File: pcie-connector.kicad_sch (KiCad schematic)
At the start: 6 parts, among them J9 Edge_Conn_Bus_PCIe_x4, SW6 SW_CVS-02B

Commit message: [#65754] Rename project
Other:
- title: SO-DIMM DDR5 Tester -> RDIMM DDR5 Tester
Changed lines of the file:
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@@
   (paper "A3")
   (title_block
-    (title "SO-DIMM DDR5 Tester")
-    (date "2024-04-23")
-    (rev "1.2.0")
+    (title "RDIMM DDR5 Tester")
+    (date "2024-09-26")
+    (rev "2.0.0")
     (comment 1 "www.antmicro.com")
     (comment 2 "Antmicro Ltd")
@@
     (pin "SH")
     (instances
-      (project "rdimm-ddr5-tester-ultrascale-plus"
+      (project "data-center-rdimm-ddr5-tester"
         (path "/1faa6543-e26a-4449-8bac-ee14b9f19e5f/fea793c3-bc28-42ef-95e7-45c2f3eee090"
           (reference "SW6") (unit 1)
@@
     (pin "1")
     (instances
-      (project "rdimm-ddr5-tester-ultrascale-plus"
+      (project "data-center-rdimm-ddr5-tester"
         (path "/1faa6543-e26a-4449-8bac-ee14b9f19e5f/fea793c3-bc28-42ef-95e7-45c2f3eee090"
           (reference "#PWR0398") (unit 1)
@@
     (pin "1")
     (instances
-      (project "rdimm-ddr5-tester-ultrascale-plus"
+      (project "data-center-rdimm-ddr5-tester"
         (path "/1faa6543-e26a-4449-8bac-ee14b9f19e5f/fea793c3-bc28-42ef-95e7-45c2f3eee090"
           (reference "#PWR0422") (unit 1)
@@
     (pin "1")
     (instances
-      (project "rdimm-ddr5-tester-ultrascale-plus"
+      (project "data-center-rdimm-ddr5-tester"
         (path "/1faa6543-e26a-4449-8bac-ee14b9f19e5f/fea793c3-bc28-42ef-95e7-45c2f3eee090"
           (reference "#PWR0402") (unit 1)
@@
     (pin "1")
     (instances
-      (project "rdimm-ddr5-tester-ultrascale-plus"
+      (project "data-center-rdimm-ddr5-tester"
         (path "/1faa6543-e26a-4449-8bac-ee14b9f19e5f/fea793c3-bc28-42ef-95e7-45c2f3eee090"
           (reference "#PWR0403") (unit 1)
@@
     (pin "2")
     (instances
-      (project "rdimm-ddr5-tester-ultrascale-plus"
+      (project "data-center-rdimm-ddr5-tester"
         (path "/1faa6543-e26a-4449-8bac-ee14b9f19e5f/fea793c3-bc28-42ef-95e7-45c2f3eee090"
           (reference "C225") (unit 1)
@@
     (pin "1")
     (instances
-      (project "rdimm-ddr5-tester-ultrascale-plus"
+      (project "data-center-rdimm-ddr5-tester"
         (path "/1faa6543-e26a-4449-8bac-ee14b9f19e5f/fea793c3-bc28-42ef-95e7-45c2f3eee090"
           (reference "#PWR0400") (unit 1)
@@
     (pin "2")
     (instances
-      (project "rdimm-ddr5-tester-ultrascale-plus"
+      (project "data-center-rdimm-ddr5-tester"
         (path "/1faa6543-e26a-4449-8bac-ee14b9f19e5f/fea793c3-bc28-42ef-95e7-45c2f3eee090"
           (reference "C224") (unit 1)
@@
     (pin "1")
     (instances
-      (project "rdimm-ddr5-tester-ultrascale-plus"
+      (project "data-center-rdimm-ddr5-tester"
         (path "/1faa6543-e26a-4449-8bac-ee14b9f19e5f/fea793c3-bc28-42ef-95e7-45c2f3eee090"
           (reference "#PWR0401") (unit 1)
@@
     (pin "1")
     (instances
-      (project "rdimm-ddr5-tester-ultrascale-plus"
+      (project "data-center-rdimm-ddr5-tester"
         (path "/1faa6543-e26a-4449-8bac-ee14b9f19e5f/fea793c3-bc28-42ef-95e7-45c2f3eee090"
           (reference "#PWR0399") (unit 1)
@@
     (pin "B9")
     (instances
-      (project "rdimm-ddr5-tester-ultrascale-plus"
+      (project "data-center-rdimm-ddr5-tester"
         (path "/1faa6543-e26a-4449-8bac-ee14b9f19e5f/fea793c3-bc28-42ef-95e7-45c2f3eee090"
           (reference "J9") (unit 1)
@@
     (pin "2")
     (instances
-      (project "rdimm-ddr5-tester-ultrascale-plus"
+      (project "data-center-rdimm-ddr5-tester"
         (path "/1faa6543-e26a-4449-8bac-ee14b9f19e5f/fea793c3-bc28-42ef-95e7-45c2f3eee090"
           (reference "R191") (unit 1)
@@
     (pin "2")
     (instances
-      (project "rdimm-ddr5-tester-ultrascale-plus"
+      (project "data-center-rdimm-ddr5-tester"
         (path "/1faa6543-e26a-4449-8bac-ee14b9f19e5f/fea793c3-bc28-42ef-95e7-45c2f3eee090"
           (reference "R192") (unit 1)

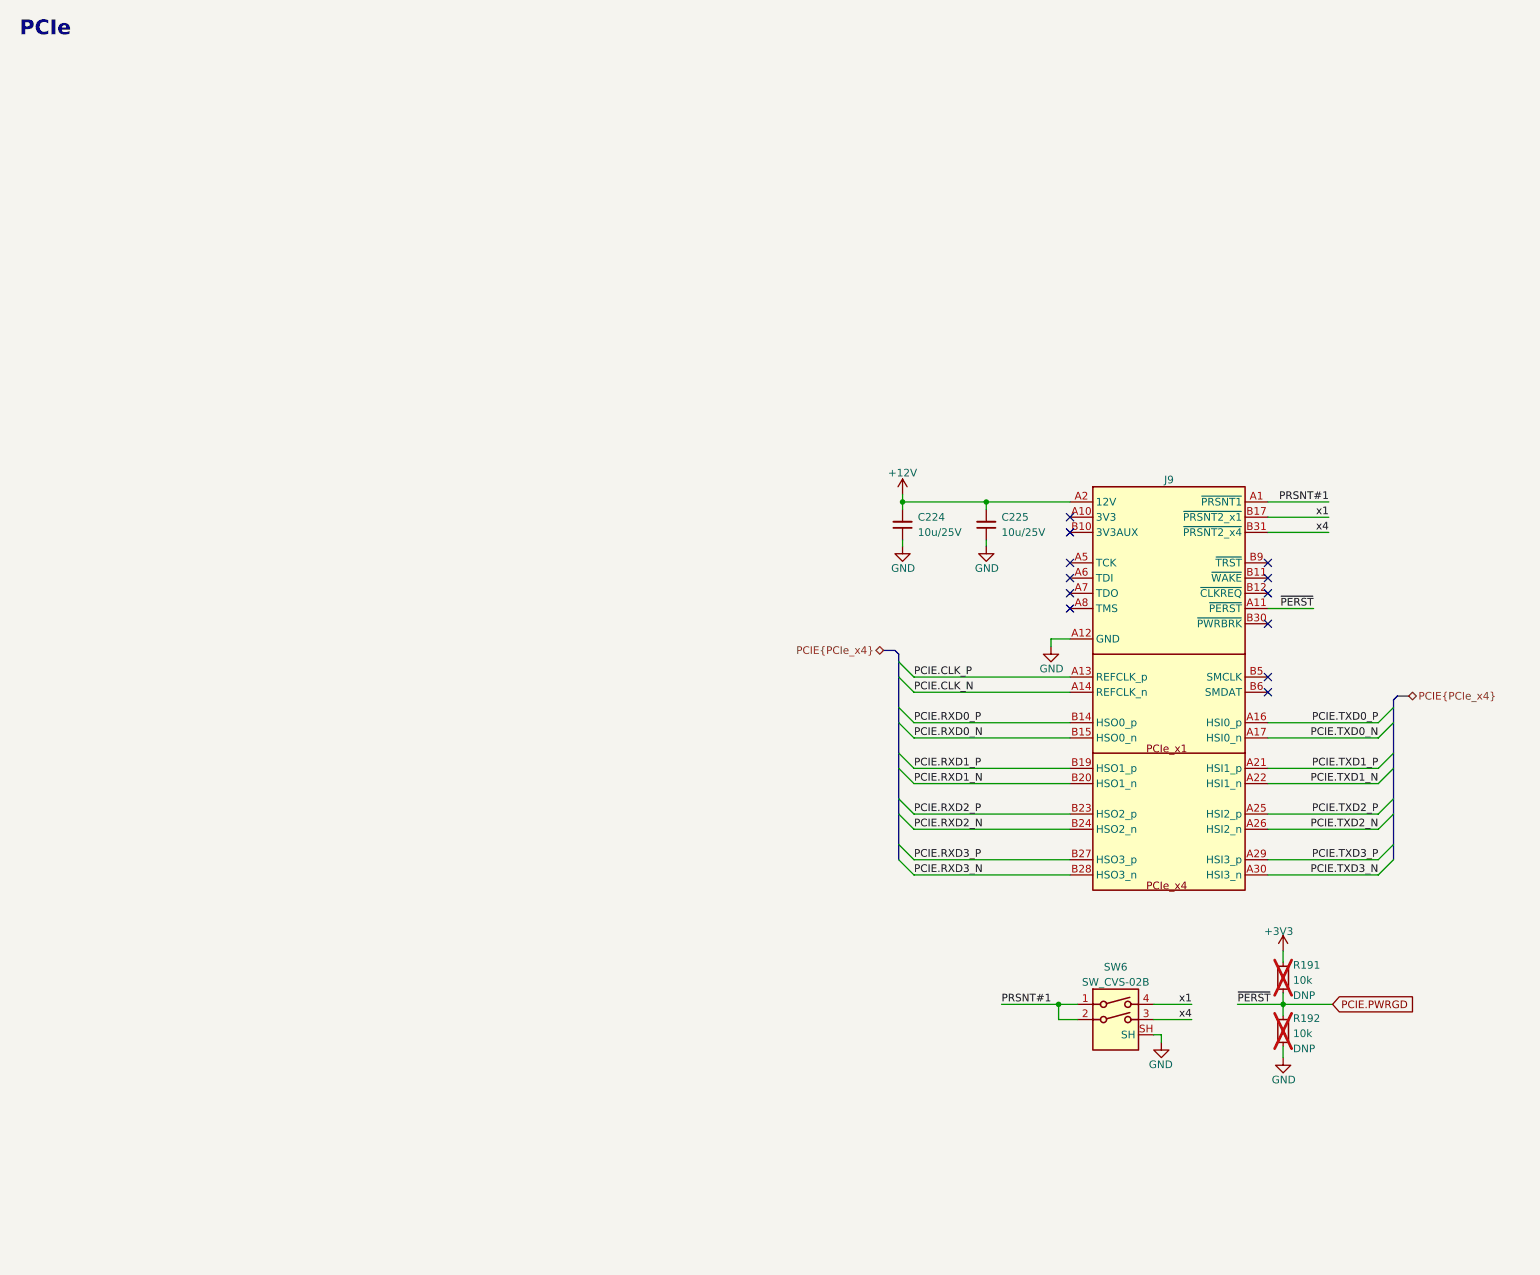
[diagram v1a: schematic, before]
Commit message: [#66312] Connect x8 PCIe
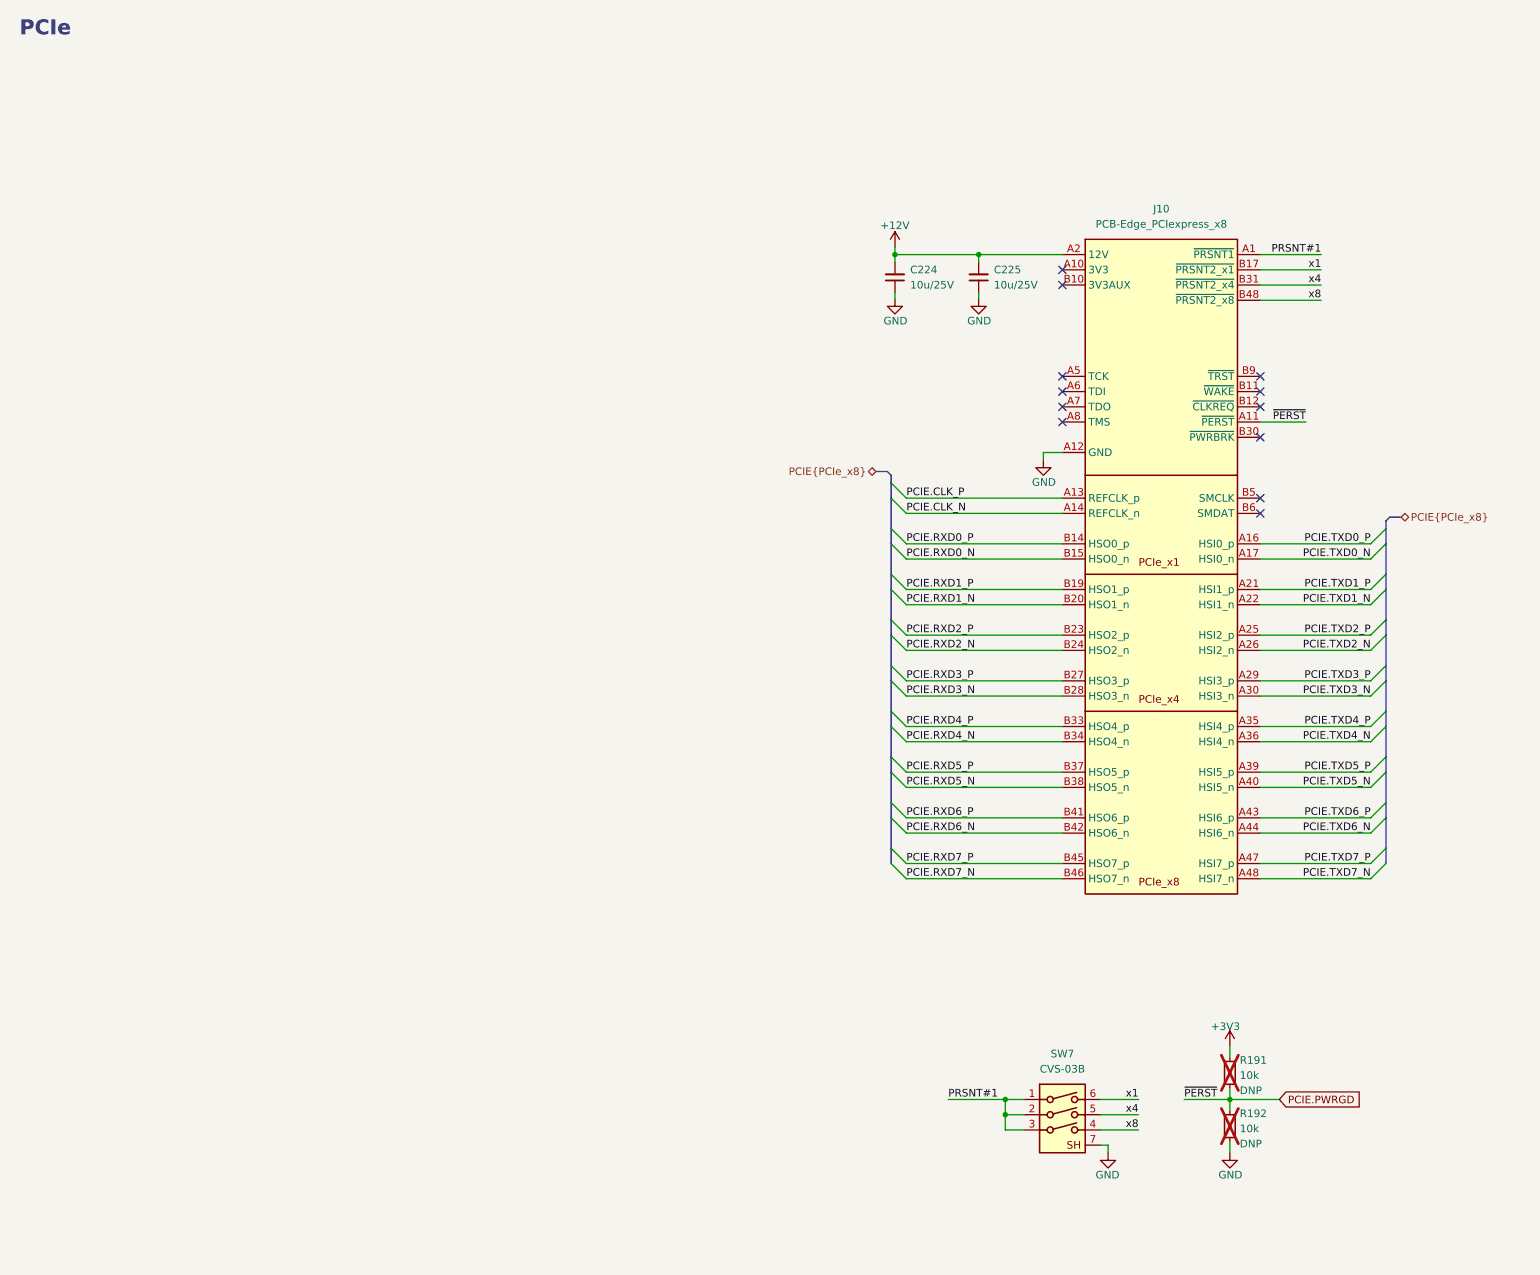
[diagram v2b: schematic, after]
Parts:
- removed J9: Edge_Conn_Bus_PCIe_x4, antmicro-footprints:Edge_Conn_Bus_PCIexpress_x4, symbol antmicroPciConnectors:Edge_Conn_Bus_PCIe_x4
- removed SW6: SW_CVS-02B, antmicro-footprints:SW_DIP_SPSTx02_Slide_Copal_CVS-02xB_W5.9mm_P1mm, symbol antmicroSlideSwitches:SW_CVS-02B
- added J10: PCB-Edge_PCIexpress_x8, antmicro-footprints:PCB-Edge_PCIexpress_x8, symbol antmicroEdgeConnectors:PCB-Edge_PCIexpress_x8
- added SW7: CVS-03B, antmicro-footprints:SW_DIP_SPSTx03_Slide_Copal_CVS-03xB_W5.9mm_P1mm, symbol antmicroSlideSwitches:CVS-03B
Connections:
- net +12V: now also J10.A2 (12V), J10.A3 (12V), J10.B1 (12V), J10.B2 (12V), J10.B3 (12V)
- net GND: now also J10.A12 (GND), J10.A15 (GND), J10.A18 (GND), J10.A20 (GND), J10.A23 (GND), J10.A24 (GND), J10.A27 (GND), J10.A28 (GND), J10.A31 (GND), J10.A34 (GND), J10.A37 (GND), J10.A38 (GND), J10.A4 (GND), J10.A41 (GND), J10.A42 (GND), J10.A45 (GND), J10.A46 (GND), J10.A49 (GND), J10.B13 (GND), J10.B16 (GND), J10.B18 (GND), J10.B21 (GND), J10.B22 (GND), J10.B25 (GND), J10.B26 (GND), J10.B29 (GND), J10.B32 (GND), J10.B35 (GND), J10.B36 (GND), J10.B39 (GND), J10.B4 (GND), J10.B40 (GND), J10.B43 (GND), J10.B44 (GND), J10.B47 (GND), J10.B49 (GND), J10.B7 (GND), SW7.7
- net PCIE.CLK_N: now also J10.A14 (REFCLK_n)
- net PCIE.CLK_P: now also J10.A13 (REFCLK_p)
- net PCIE.PWRGD: now also J10.A11 (~{PERST})
- net PCIE.RXD0_N: now also J10.B15 (HSO0_n)
- net PCIE.RXD0_P: now also J10.B14 (HSO0_p)
- net PCIE.RXD1_N: now also J10.B20 (HSO1_n)
- net PCIE.RXD1_P: now also J10.B19 (HSO1_p)
- net PCIE.RXD2_N: now also J10.B24 (HSO2_n)
- net PCIE.RXD2_P: now also J10.B23 (HSO2_p)
- net PCIE.RXD3_N: now also J10.B28 (HSO3_n)
- net PCIE.RXD3_P: now also J10.B27 (HSO3_p)
- net PCIE.TXD0_N: now also J10.A17 (HSI0_n)
- net PCIE.TXD0_P: now also J10.A16 (HSI0_p)
- net PCIE.TXD1_N: now also J10.A22 (HSI1_n)
- net PCIE.TXD1_P: now also J10.A21 (HSI1_p)
- net PCIE.TXD2_N: now also J10.A26 (HSI2_n)
- net PCIE.TXD2_P: now also J10.A25 (HSI2_p)
- net PCIE.TXD3_N: now also J10.A30 (HSI3_n)
- net PCIE.TXD3_P: now also J10.A29 (HSI3_p)
- net PRSNT#1: now also J10.A1 (~{PRSNT1}), SW7.1, SW7.2, SW7.3
- net x1: now also J10.B17 (~{PRSNT2_x1}), SW7.6
- net x4: now also J10.B31 (~{PRSNT2_x4}), SW7.5
- new net: J10.A10 (3V3), J10.A9 (3V3), J10.B8 (3V3)
- new net PCIE.RXD4_N: J10.B34 (HSO4_n)
- new net PCIE.RXD4_P: J10.B33 (HSO4_p)
- new net PCIE.RXD5_N: J10.B38 (HSO5_n)
- new net PCIE.RXD5_P: J10.B37 (HSO5_p)
- new net PCIE.RXD6_N: J10.B42 (HSO6_n)
- new net PCIE.RXD6_P: J10.B41 (HSO6_p)
- new net PCIE.RXD7_N: J10.B46 (HSO7_n)
- new net PCIE.RXD7_P: J10.B45 (HSO7_p)
- new net PCIE.TXD4_N: J10.A36 (HSI4_n)
- new net PCIE.TXD4_P: J10.A35 (HSI4_p)
- new net PCIE.TXD5_N: J10.A40 (HSI5_n)
- new net PCIE.TXD5_P: J10.A39 (HSI5_p)
- new net PCIE.TXD6_N: J10.A44 (HSI6_n)
- new net PCIE.TXD6_P: J10.A43 (HSI6_p)
- new net PCIE.TXD7_N: J10.A48 (HSI7_n)
- new net PCIE.TXD7_P: J10.A47 (HSI7_p)
- new net x8: J10.B48 (~{PRSNT2_x8}), SW7.4
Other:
- moved on the sheet: C224, C225, R191, R192

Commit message: [#67725] Clean-up PCIe sheet
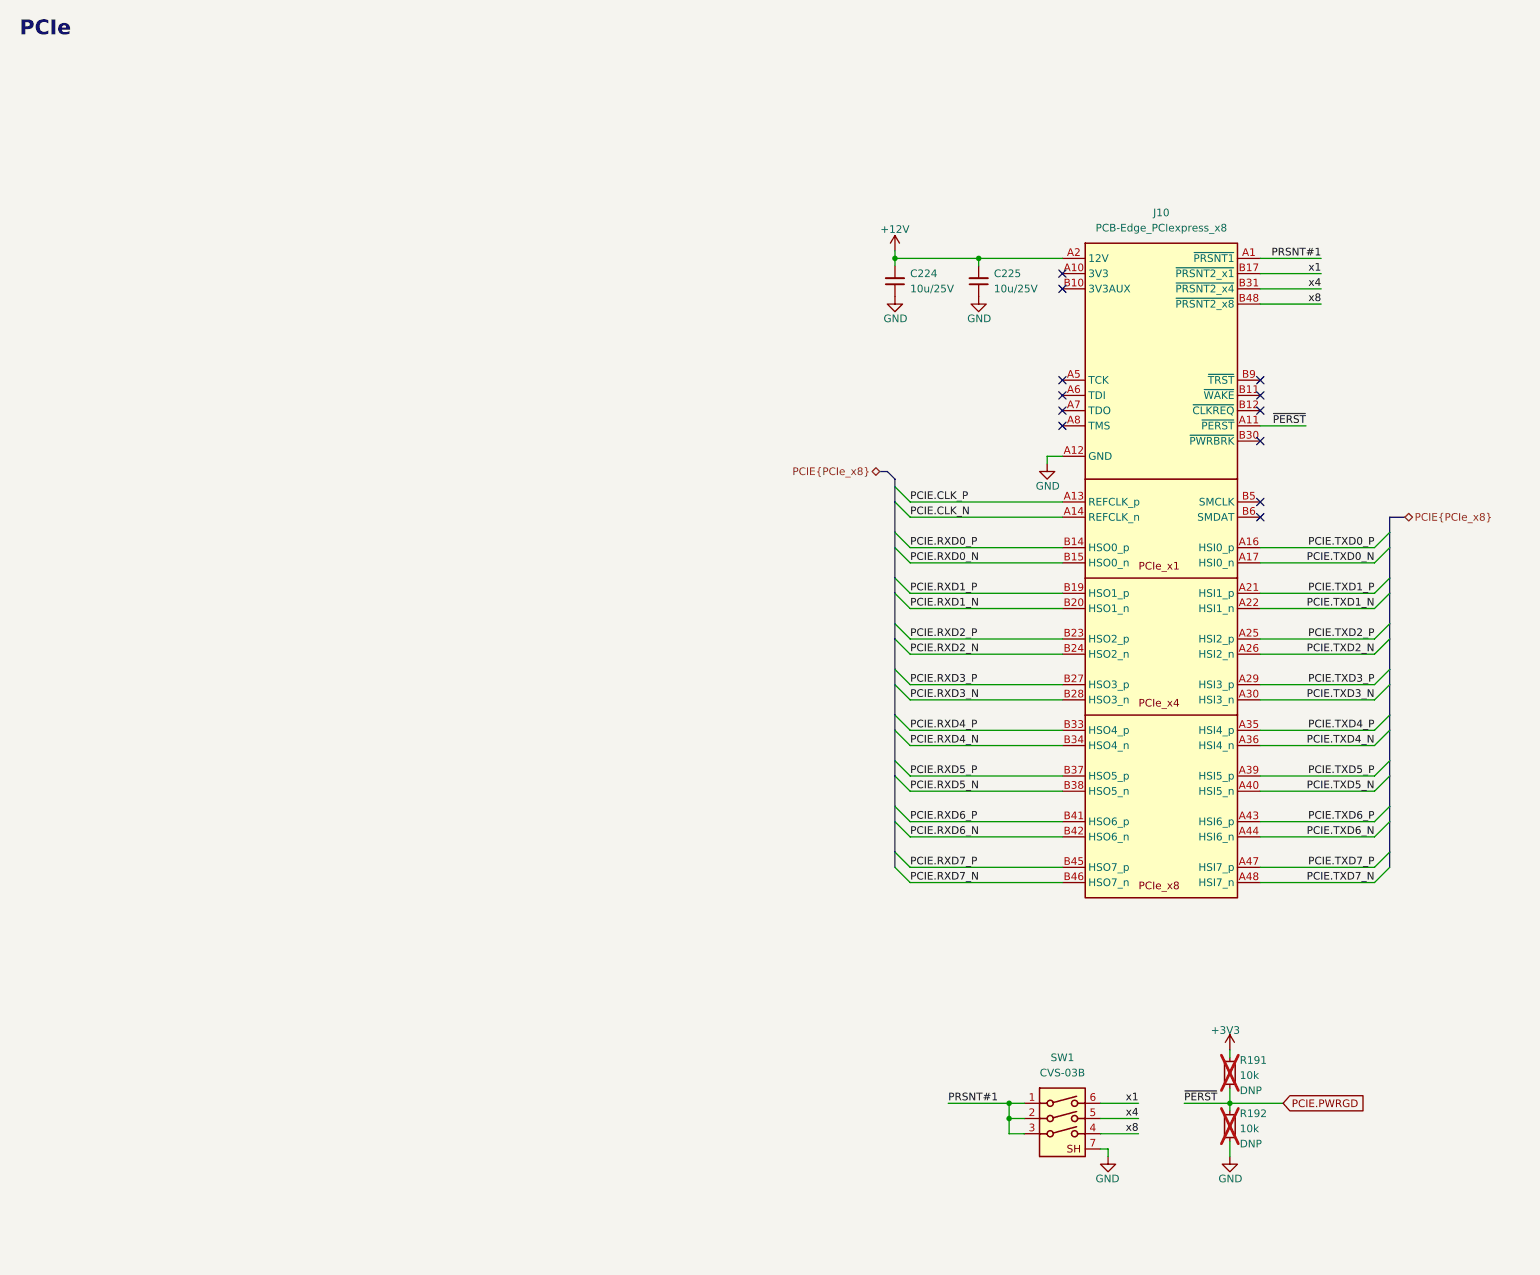
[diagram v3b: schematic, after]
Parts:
- removed SW7: CVS-03B, antmicro-footprints:SW_DIP_SPSTx03_Slide_Copal_CVS-03xB_W5.9mm_P1mm, symbol antmicroSlideSwitches:CVS-03B
- added SW1: CVS-03B, antmicro-footprints:SW_DIP_SPSTx03_Slide_Copal_CVS-03xB_W5.9mm_P1mm, symbol antmicroSlideSwitches:CVS-03B
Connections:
- net GND: now also SW1.7
- net PRSNT#1: now also SW1.1, SW1.2, SW1.3
- net x1: now also SW1.6
- net x4: now also SW1.5
- net x8: now also SW1.4
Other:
- moved on the sheet: C224, C225

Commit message: [#68016] Clean-up the schematic
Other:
- moved on the sheet: C224, C225, J10, R191, R192, SW1

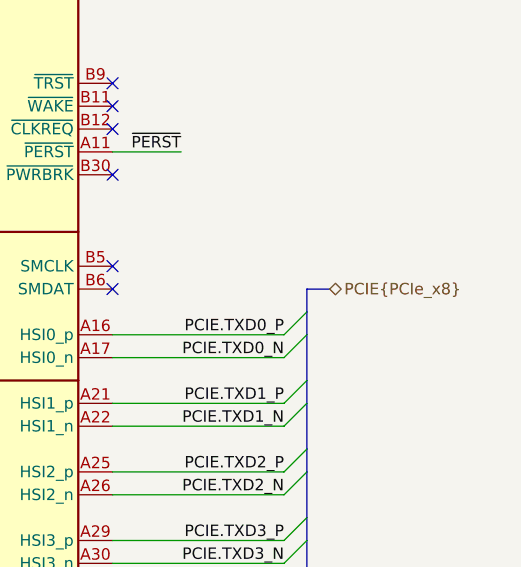
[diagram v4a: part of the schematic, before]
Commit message: [#68016] Improve bus entry marking
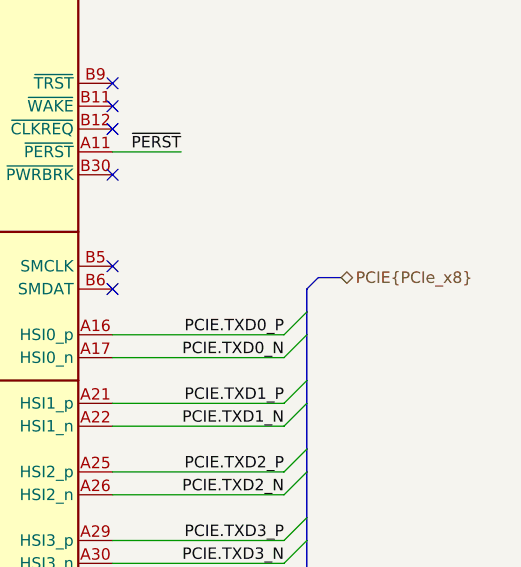
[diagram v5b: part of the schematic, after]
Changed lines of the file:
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@@
     (stroke (width 0) (type default))
   )
-  (bus (pts (xy 250.19 111.76) (xy 247.65 111.76))
+  (bus (pts (xy 251.46 110.49) (xy 248.92 110.49))
     (stroke (width 0) (type default))
   )
@@
   )
   (wire (pts (xy 236.22 68.58) (xy 226.06 68.58))
+    (stroke (width 0) (type default))
+  )
+  (bus (pts (xy 247.65 111.76) (xy 248.92 110.49))
     (stroke (width 0) (type default))
   )
@@
     )
   )
-  (hierarchical_label "PCIE{PCIe_x8}" (shape bidirectional) (at 250.19 111.76 0) (fields_autoplaced)
+  (hierarchical_label "PCIE{PCIe_x8}" (shape bidirectional) (at 251.46 110.49 0) (fields_autoplaced)
     (effects (font (size 1.27 1.27)) (justify left))
   )
